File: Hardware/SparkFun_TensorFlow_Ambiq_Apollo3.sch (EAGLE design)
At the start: 102 parts, among them J5 CORTEX_DEBUG_PTH, J6 CAMERA-OV7670, M1 MEMS_MIC, M2 MEMS_MIC, U1 AMBIQ-APOLLO3KBR, U2 LIS2DH12, U3 1.8V, U4 LMV358, Y1 32MHz, Y2 32.768kHz

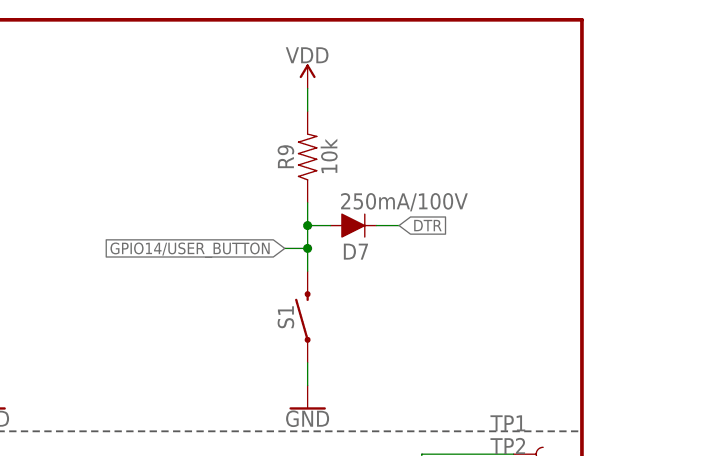
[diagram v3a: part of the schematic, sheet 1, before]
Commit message: Moving designators for asm sheet
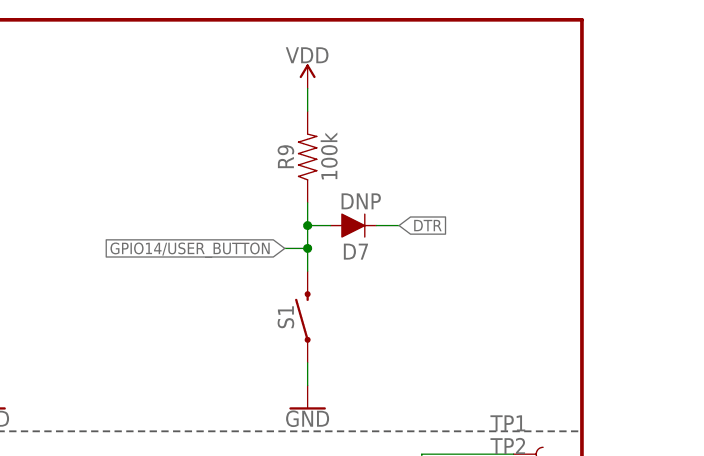
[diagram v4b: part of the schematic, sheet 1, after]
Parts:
- D7: value 250mA/100V -> DNP
- R9: value 10k -> 100k
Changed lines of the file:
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@@
 <?xml version="1.0" encoding="utf-8"?>
 <!DOCTYPE eagle SYSTEM "eagle.dtd">
-<eagle version="9.1.3">
+<eagle version="9.3.0">
 <drawing>
 <settings>
@@
 <part name="GND27" library="SparkFun-PowerSymbols" deviceset="GND" device=""/>
 <part name="GND26" library="SparkFun-PowerSymbols" deviceset="GND" device=""/>
-<part name="R9" library="SparkFun-Resistors" deviceset="10KOHM" device="-0402_TIGHT-1/10W-1%" value="10k"/>
+<part name="R9" library="SparkFun-Resistors" deviceset="10KOHM" device="-0402_TIGHT-1/10W-1%" value="100k"/>
 <part name="SUPPLY15" library="SparkFun-PowerSymbols" deviceset="VDD" device=""/>
 <part name="D4" library="SparkFun-LED" deviceset="LED-BLUE" device="0603" value="BLUE"/>
@@
 <part name="TP6" library="SparkFun-Connectors" deviceset="TEST-POINT" device="3X5"/>
 <part name="TP7" library="SparkFun-Connectors" deviceset="TEST-POINT" device="3X5"/>
-<part name="D7" library="SparkFun-DiscreteSemi" deviceset="DIODE" device="-BAS16J" value="250mA/100V"/>
+<part name="D7" library="SparkFun-DiscreteSemi" deviceset="DIODE" device="-BAS16J" value="DNP"/>
 </parts>
 <sheets>

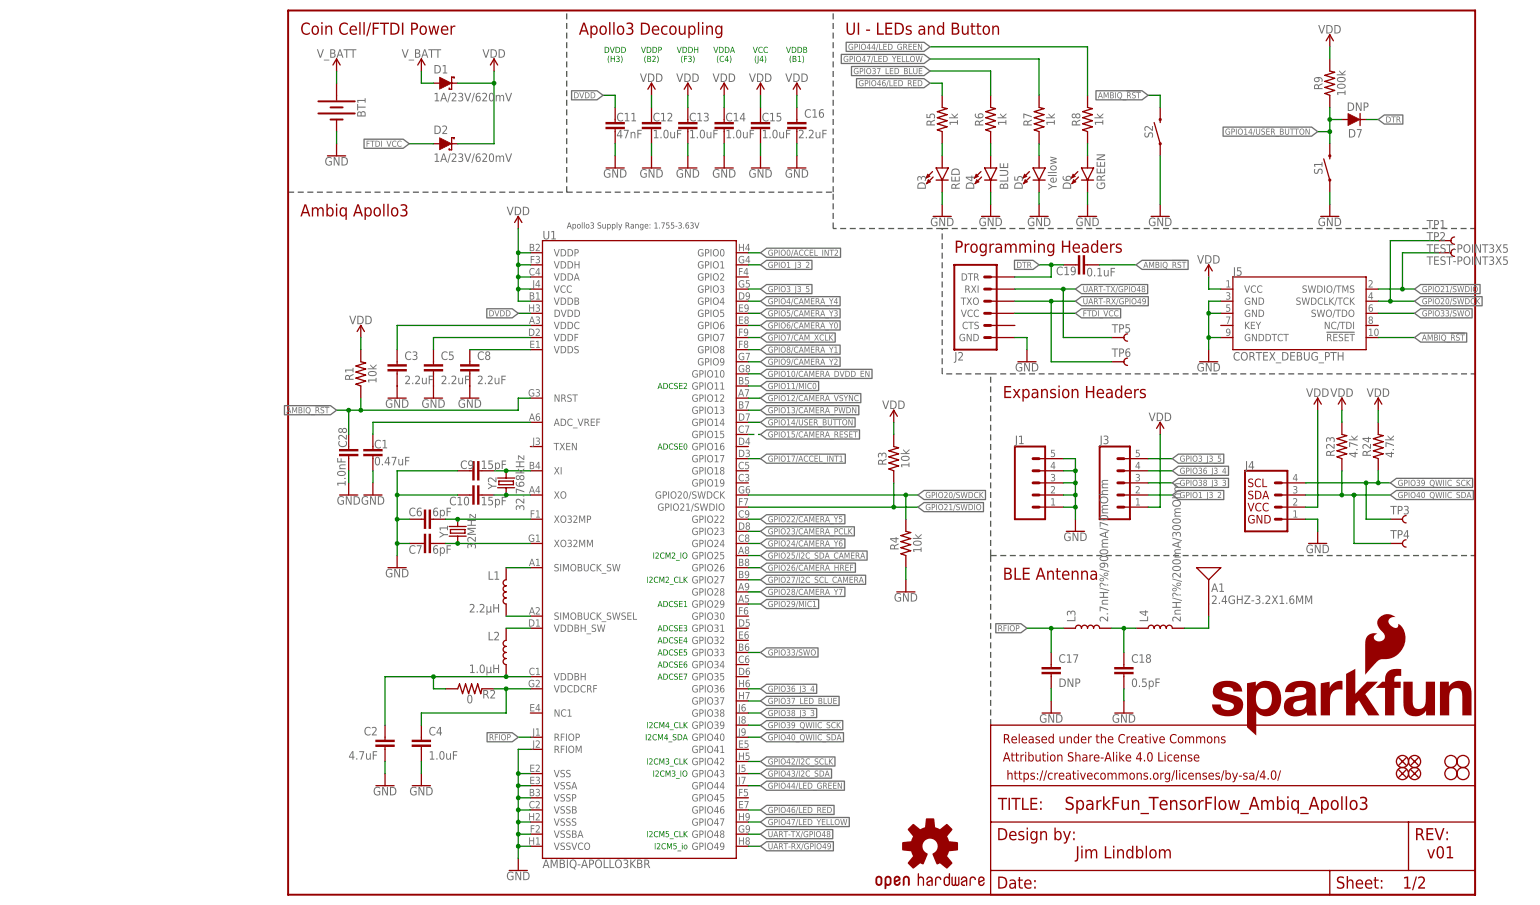
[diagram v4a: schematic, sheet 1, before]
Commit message: Change to module layout
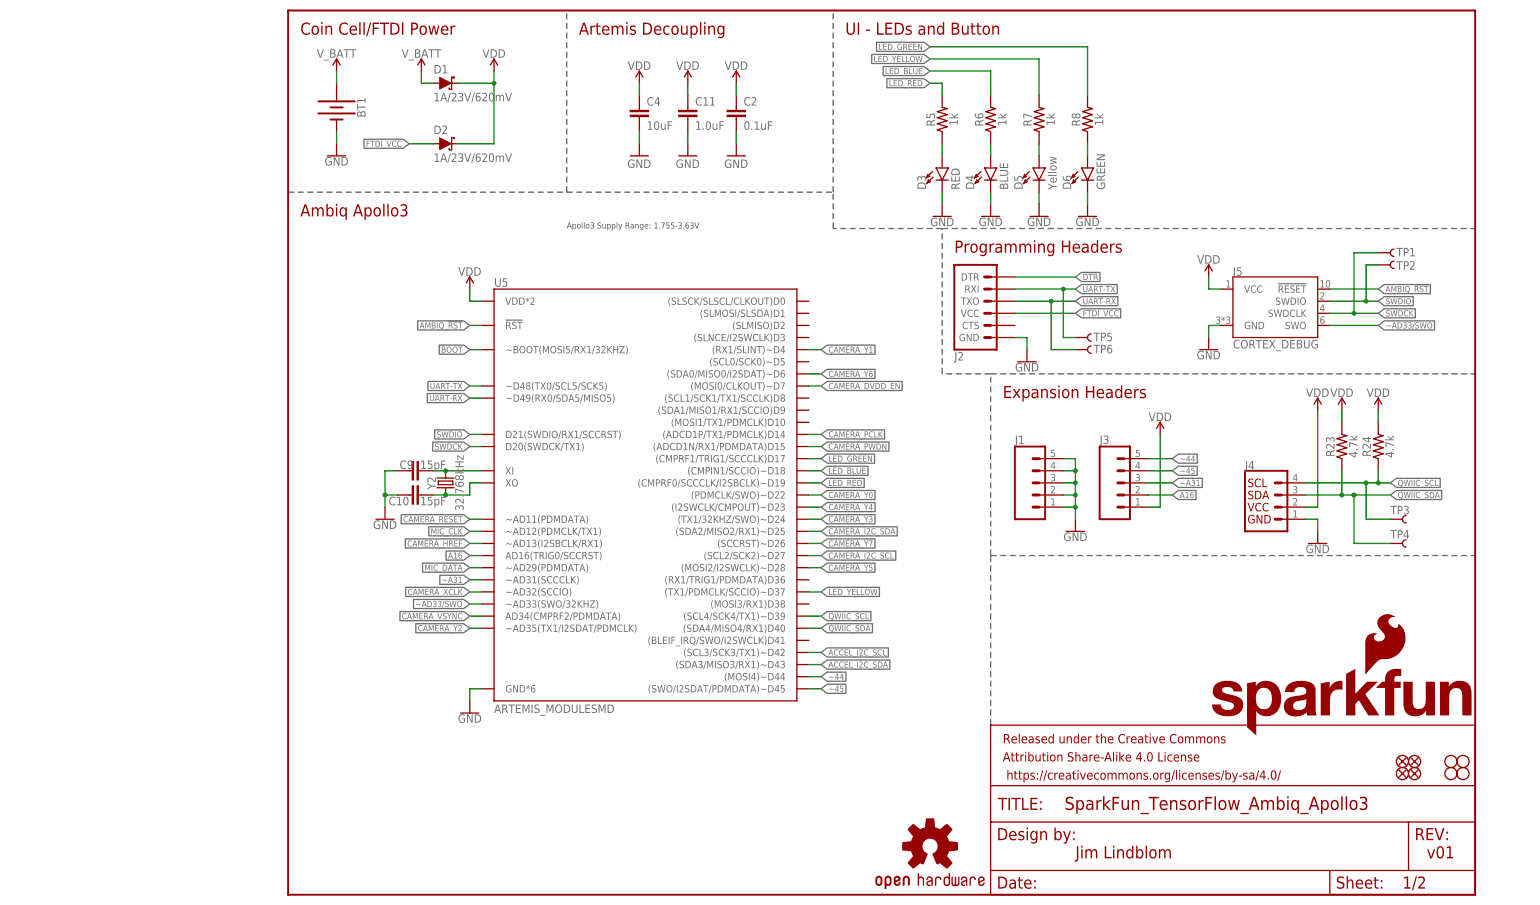
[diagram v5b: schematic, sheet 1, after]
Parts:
- removed A1: 2.4GHZ-3.2X1.6MM, ambiq:ANTENNA-2.4GHZ-3.2X1.6MM
- removed C12, C13, C14, C15: 1.0uF, ambiq:1.0UF-0402-TIGHT-16V-10%
- removed C16, C3, C5, C8: 2.2uF, SparkFun-Capacitors:2.2UF-0402_TIGHT-10V-10%-X5R
- removed C19, C25, C27: 0.1uF, ambiq:0.1UF-0402-TIGHT-16V-10%
- removed C24, C26: 4.7uF, SparkFun-Capacitors:4.7UF-0603-6.3V-(10%)
- removed C28: 1.0nF, SparkFun-Capacitors:1.0NF/1000PF-0402_TIGHT-50V-10%
- removed D7: DNP, SparkFun-DiscreteSemi:DIODE-BAS16J
- removed L1: 2.2μH, SparkFun-Coils:2.2μH-0805_WIDE-2.2μH-1.7A-0.14OHM
- removed L2: 1.0μH, SparkFun-Coils:1.0μH-0805_WIDE-1.0μH-1.4A-0.07OHM
- removed L3: 2.7nH/?%/900mA/70mOhm, SparkFun-Coils:INDUCTOR-0402_TIGHT-2.7NH
- removed L4: 2nH/?%/200mA/300mOhm, SparkFun-Coils:INDUCTOR-0402_TIGHT-2.0NH
- removed M1, M2: MEMS_MIC, SparkFun-Sensors:MEMS_MICROPHONESPW2430HR5H-B
- removed R1, R19, R3, R4: 10k, SparkFun-Resistors:10KOHM-0402_TIGHT-1/10W-1%
- removed R16, R17: 10k, SparkFun-Resistors:10KOHM-0603-1/10W-1%
- removed R18: 22k, SparkFun-Resistors:22KOHM-0402_TIGHT-1/10W-1%
- removed R2: 0, SparkFun-Resistors:0OHM-0402_TIGHT-1/16W
- removed R20, R21: 750K, SparkFun-Resistors:750KOHM-0603-1/10W-1%
- removed R9: 100k, SparkFun-Resistors:10KOHM-0402_TIGHT-1/10W-1%
- removed S1, S2: MOMENTARY-SWITCH-SPST-SMD-5.2-TALL-REDUNDANT, SparkFun-Switches:MOMENTARY-SWITCH-SPST-SMD-5.2-TALL-REDUNDANT
- removed U1: AMBIQ-APOLLO3KBR, SparkFun-IC-Microcontroller:AMBIQ-APOLLO3KBR
- removed U4: LMV358, SparkFun-IC-Amplifiers:LMV358SOIC
- removed Y1: 32MHz, SparkFun-Clocks:CRYSTAL-32MHZ-SMD-2.0X1.6MM
- added E1, E2: SPH0641LM4H-1, SparkFun-Sensors:SPH0641LM4H-1_MICROPHONE
- added R27, R29: 100k, SparkFun-Resistors:100KOHM-0603-1/10W-1%
- added R28: 10k, SparkFun-Resistors:10KOHM-0603-1/10W-1%
- added S3: RESET, SparkFun-Switches:MOMENTARY-SWITCH-SPST-SMD-5.2MM-TALL
- added U5: ARTEMIS_MODULESMD, Testing:ARTEMIS_MODULESMD
- C1: value 0.47uF -> 0.1uF; device SparkFun-Capacitors:470NF-0402_TIGHT-6.3V-10%-X5R -> ambiq:0.1UF-0402-TIGHT-16V-10%
- C11: value 47nF -> 1.0uF; device SparkFun-Capacitors:47NF-0402_TIGHT-25V-10%-X7R -> SparkFun-Capacitors:1.0UF-0402T-16V-10%
- C17: value DNP -> 1nF; device ambiq:DNP-CAP-0402-TIGHT -> SparkFun-Capacitors:1.0NF/1000PF-0603-50V-10%
- C18: value 0.5pF -> 0.1uF; device SparkFun-Capacitors:0.5PF-0402_TIGHT-20V-PM0.05PF-NP0 -> ambiq:0.1UF-0402-TIGHT-16V-10%
- C2: value 4.7uF -> 0.1uF; device SparkFun-Capacitors:4.7UF-0402_TIGHT-6.3V-20%-X5R -> SparkFun-Capacitors:0.1UF-0402T-16V-10%
- C4: value 1.0uF -> 10uF; device ambiq:1.0UF-0402-TIGHT-16V-10% -> SparkFun-Capacitors:10UF-0603-6.3V-20%
- C6: value 6pF -> 0.1uF; device ambiq:6PF-0402-TIGHT-50V-0.5% -> SparkFun-Capacitors:0.1UF-0603-25V-5%
- C7: value 6pF -> 2.2uF; device ambiq:6PF-0402-TIGHT-50V-0.5% -> SparkFun-Capacitors:2.2UF-0603-10V-20%
- J5: value CORTEX_DEBUG_PTH -> CORTEX_DEBUG; device SparkFun-Connectors:CORTEX_DEBUG_PTH -> SparkFun-Connectors:CORTEX_DEBUG_MINIMUM_PTH_NS
- R10, R11, R22, R25, R26: device SparkFun-Resistors:10KOHM-0402_TIGHT-1/10W-1% -> SparkFun-Resistors:10KOHM-0402T-1/16W-1%
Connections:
- removed net ADC_VREF: C1.1, U1.ADC_VREF
- removed net DTR: C19.1, D7.C, J2.DTR
- removed net DVDD: C11.1, U1.DVDD
- removed net GPIO0/ACCEL_INT2: R25.2, U1.GPIO0, U2.INT2
- removed net GPIO10/CAMERA_DVDD_EN: R11.2, U1.GPIO10, U3.EN
- removed net GPIO11/MIC0: R21.1, U1.GPIO11, U4G1.OUT
- removed net GPIO12/CAMERA_VSYNC: J6.VSYNC, U1.GPIO12
- removed net GPIO13/CAMERA_PWDN: J6.PWDN, R22.2, U1.GPIO13
- removed net GPIO14/USER_BUTTON: D7.A, R9.1, S1.2, U1.GPIO14
- removed net GPIO15/CAMERA_RESET: J6.RESET, R10.1, U1.GPIO15
- removed net GPIO17/ACCEL_INT1: R26.2, U1.GPIO17, U2.INT1
- removed net GPIO1_J3_2: J3.2, U1.GPIO1
- removed net GPIO20/SWDCK: J5.SWDCLK/TCK, R4.2, TP1.1, U1.GPIO20/SWDCK
- removed net GPIO21/SWDIO: J5.SWDIO/TMS, R3.1, TP2.1, U1.GPIO21/SWDIO
- removed net GPIO22/CAMERA_Y5: J6.Y5, U1.GPIO22
- removed net GPIO23/CAMERA_PCLK: J6.PCLK, U1.GPIO23
- removed net GPIO24/CAMERA_Y6: J6.Y6, U1.GPIO24
- removed net GPIO25/I2C_SDA_CAMERA: J6.SIO_D, R15.1, U1.GPIO25
- removed net GPIO26/CAMERA_HREF: J6.HREF, U1.GPIO26
- removed net GPIO27/I2C_SCL_CAMERA: J6.SIO_C, R13.1, U1.GPIO27
- removed net GPIO28/CAMERA_Y7: J6.Y7, U1.GPIO28
- removed net GPIO29/MIC1: R20.1, U1.GPIO29, U4G2.OUT
- removed net GPIO33/SWO: J5.SWO/TDO, U1.GPIO33
- removed net GPIO36_J3_4: J3.4, U1.GPIO36
- removed net GPIO37_LED_BLUE: R6.2, U1.GPIO37
- removed net GPIO38_J3_3: J3.3, U1.GPIO38
- removed net GPIO39_QWIIC_SCK: J4.4, R24.1, TP3.1, U1.GPIO39
- removed net GPIO3_J3_5: J3.5, U1.GPIO3
- removed net GPIO4/CAMERA_Y4: J6.Y4, U1.GPIO4
- removed net GPIO40_QWIIC_SDA: J4.3, R23.1, TP4.1, U1.GPIO40
- removed net GPIO42/I2C_SCLK: R12.1, U1.GPIO42, U2.SCL/SPC
- removed net GPIO43/I2C_SDA: R14.1, U1.GPIO43, U2.SDA/SDI/SDO
- removed net GPIO44/LED_GREEN: R8.2, U1.GPIO44
- removed net GPIO46/LED_RED: R5.2, U1.GPIO46
- removed net GPIO47/LED_YELLOW: R7.2, U1.GPIO47
- removed net GPIO5/CAMERA_Y3: J6.Y3, U1.GPIO5
- removed net GPIO6/CAMERA_Y0: J6.Y0, U1.GPIO6
- removed net GPIO7/CAM_XCLK: J6.XCLK1, U1.GPIO7
- removed net GPIO8/CAMERA_Y1: J6.Y1, U1.GPIO8
- removed net GPIO9/CAMERA_Y2: J6.Y2, U1.GPIO9
- removed net MIC0_OUT: C24.1, M1.OUT
- removed net MIC1_OUT: C26.1, M2.OUT
- removed net N$1: A1.SIGNAL, L4.2
- removed net N$10: C24.2, R16.2
- removed net N$11: R17.1, R20.2, U4G2.-IN
- removed net N$12: R16.1, R21.2, U4G1.-IN
- removed net N$14: C26.2, R17.2
- removed net N$16: C18.1, L3.2, L4.1
- removed net N$3: C6.2, U1.XO32MP, Y1.2
- removed net N$9: R18.1, R19.2, U4G1.+IN, U4G2.+IN
- removed net RFIOP: C17.1, L3.1, U1.RFIOP
- removed net SIMBUCK_SWSEL: L1.2, U1.SIMOBUCK_SWSEL
- removed net SIMOBUCK_SW: L1.1, U1.SIMOBUCK_SW
- removed net UART-RX/GPIO49: J2.TXO, TP6.1, U1.GPIO49
- removed net UART-TX/GPIO48: J2.RXI, TP5.1, U1.GPIO48
- removed net VDCDCRF: C4.1, R2.2, U1.VDCDCRF
- removed net VDDBH: C2.1, L2.2, R2.1, U1.VDDBH
- removed net VDDBH_SW: L2.1, U1.VDDBH_SW
- removed net VDDC: C3.1, U1.VDDC
- removed net VDDF: C5.1, U1.VDDF
- removed net VDDS: C8.1, U1.VDDS
- removed net XI: C9.2, U1.XI, Y2.2
- new net !DTR: C6.1, C7.1, J2.DTR, R29.2
- new net A16: J3.2, U5.AD16(TRIG0/SCCRST)
- new net ACCEL_I2C_SCL: R12.1, U2.SCL/SPC, U5.(SCL3/SCK3/TX1)~D42
- new net ACCEL_I2C_SDA: R14.1, U2.SDA/SDI/SDO, U5.(SDA3/MISO3/RX1)~D43
- new net ACCEL_INT1: R26.2, U2.INT1
- new net ACCEL_INT2: R25.2, U2.INT2
- new net BOOT: C7.2, R28.2, U5.~BOOT(MOSI5/RX1/32KHZ)
- new net CAMERA_DVDD_EN: R11.2, U3.EN, U5.(MOSI0/CLKOUT)~D7
- new net CAMERA_HREF: J6.HREF, U5.~AD13(I2SBCLK/RX1)
- new net CAMERA_I2C_SCL: J6.SIO_C, R13.1, U5.(SCL2/SCK2)~D27
- new net CAMERA_I2C_SDA: J6.SIO_D, R15.1, U5.(SDA2/MISO2/RX1)~D25
- new net CAMERA_PCLK: J6.PCLK, U5.(ADCD1P/TX1/PDMCLK)D14
- new net CAMERA_PWDN: J6.PWDN, R22.2, U5.(ADCD1N/RX1/PDMDATA)D15
- new net CAMERA_RESET: J6.RESET, R10.1, U5.~AD11(PDMDATA)
- new net CAMERA_VSYNC: J6.VSYNC, U5.AD34(CMPRF2/PDMDATA)
- new net CAMERA_XCLK: J6.XCLK1, U5.~AD32(SCCIO)
- new net CAMERA_Y0: J6.Y0, U5.(PDMCLK/SWO)~D22
- new net CAMERA_Y1: J6.Y1, U5.(RX1/SLINT)~D4
- new net CAMERA_Y2: J6.Y2, U5.~AD35(TX1/I2SDAT/PDMCLK)
- new net CAMERA_Y3: J6.Y3, U5.(TX1/32KHZ/SWO)~D24
- new net CAMERA_Y4: J6.Y4, U5.(I2SWCLK/CMPOUT)~D23
- new net CAMERA_Y5: J6.Y5, U5.(MOSI2/I2SWCLK)~D28
- new net CAMERA_Y6: J6.Y6, U5.(SDA0/MISO0/I2SDAT)~D6
- new net CAMERA_Y7: J6.Y7, U5.(SCCRST)~D26
- new net LED_BLUE: R6.2, U5.(CMPIN1/SCCIO)~D18
- new net LED_GREEN: R8.2, U5.(CMPRF1/TRIG1/SCCCLK)D17
- new net LED_RED: R5.2, U5.(CMPRF0/SCCCLK/I2SBCLK)~D19
- new net LED_YELLOW: R7.2, U5.(TX1/PDMCLK/SCCIO)~D37
- new net MIC_CLK: E1.CLK, E2.CLK, U5.~AD12(PDMCLK/TX1)
- new net MIC_DATA: E1.DATA, E2.DATA, U5.~AD29(PDMDATA)
- new net QWIIC_SCL: J4.4, R24.1, TP3.1, U5.(SCL4/SCK4/TX1)~D39
- new net QWIIC_SDA: J4.3, R23.1, TP4.1, U5.(SDA4/MISO4/RX1)D40
- new net SWDCK: J5.SWDCLK, TP1.1, U5.D20(SWDCK/TX1)
- new net SWDIO: J5.SWDIO, TP2.1, U5.D21(SWDIO/RX1/SCCRST)
- new net UART-RX: J2.TXO, TP6.1, U5.~D49(RX0/SDA5/MISO5)
- new net UART-TX: J2.RXI, TP5.1, U5.~D48(TX0/SCL5/SCK5)
- new net ~44: J3.5, U5.(MOSI4)~D44
- new net ~45: J3.4, U5.(SWO/I2SDAT/PDMDATA)~D45
- new net ~A31: J3.3, U5.~AD31(SCCCLK)
- new net ~AD33/SWO: J5.SWO, U5.~AD33(SWO/32KHZ)
- net AMBIQ_!RST: now also C17.1, C6.2, R27.1, S3.2, U5.!RST; no longer C19.2, C28.1, R1.1, S2.2, U1.NRST
- net GND: now also C2.1, E1.GND, E1.SEL, E2.GND, J5.GND, R28.1, R29.1, S3.1, U5.GND*6; no longer C12.2, C13.2, C14.2, C15.2, C16.2, C2.2, C25.2, C27.2, C28.2, C3.2, C5.2, C6.1, C7.1, C8.2, J5.GND@3, J5.GND@5, J5.GNDDTCT, M1.GND, M2.GND, R19.1, R4.1, S1.1, S2.1, U1.RFIOM, U1.VSS, U1.VSSA, U1.VSSB, U1.VSSBA, U1.VSSP, U1.VSSS, U1.VSSVCO, U4G3.P$V-
- net N$2: now also C9.2, U5.XI, Y2.2; no longer C7.2, U1.XO32MM, Y1.1
- net VDD: now also C1.1, C11.1, C18.1, C2.2, C4.1, E1.VDD, E2.SEL, E2.VDD, R27.2, U5.VDD*2; no longer C12.1, C13.1, C14.1, C15.1, C16.1, C25.1, C27.1, M1.VDD, M2.VDD, R1.2, R18.2, R3.2, R9.2, U1.VCC, U1.VDDA, U1.VDDB, U1.VDDH, U1.VDDP, U4G3.P$V+
- net X0: now also U5.XO; no longer U1.XO
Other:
- note added: "Artemis Decoupling"
- note added: "Bootloader Reset Circuit"
- note added: "MEMS Microphone"
- note removed: "ADCSE0"
- note removed: "ADCSE1"
- note removed: "ADCSE2"
- note removed: "ADCSE3"
- note removed: "ADCSE4"
- note removed: "ADCSE5"
- note removed: "ADCSE6"
- note removed: "ADCSE7"
- note removed: "Apollo3 Decoupling"
- note removed: "BLE Antenna"
- note removed: "DVDD (H3)"
- note removed: "I2CM2_CLK"
- note removed: "I2CM2_IO"
- note removed: "I2CM3_CLK"
- note removed: "I2CM3_IO"
- note removed: "I2CM4_CLK"
- note removed: "I2CM4_SDA"
- note removed: "I2CM5_CLK"
- note removed: "I2CM5_io"
- note removed: "MEMS Microphone - Knowles PW2430HR5H-B"
- note removed: "Microphone Pre-Amp"
- note removed: "VCC (J4)"
- note removed: "VDDA (C4)"
- note removed: "VDDB (B1)"
- note removed: "VDDH (F3)"
- note removed: "VDDP (B2)"
- moved on the sheet: C10, C11, C2, C4, C9, TP1, TP2, TP5, TP6, Y2

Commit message: Update silk
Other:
- note added: "Camera"
- note added: "LEDs"
- note removed: "OV7670 VGA Camera"
- note removed: "UI - LEDs and Button"
- moved on the sheet: C11, C17, C2, C20, C21, C22, C23, C4, C6, C7, D3, D4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
